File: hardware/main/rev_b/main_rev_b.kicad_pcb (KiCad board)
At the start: 4 copper layers, 140 x 100 mm, 165 parts, among them J1 USB-C USB2, J10 SWD, J2 ESC_CAN_POWER, J30 GNSS_UFL, J40 915MHz_ANT, Q30 2N7002, U1 USBLC6-2SC6, U10 RP2354B, U2 TLV62569DBVR, U20 ICM-42688-P, U21 LSM6DSO32TR, U22 LPS22DFTR, U3 TLV75528PDBVR, U30 LG77LICMD, U4 TLV75533PDBVR, U40 CC1121RHBR, U41 CC1190RGVR, U50 TCAN3413DR, U51 MCP2518FD-H/QBB, Y1 12MHz ABM8-272-T3, Y40 32MHz NT2016SA-32M-TEE3017A, Y50 40MHz ABM8G

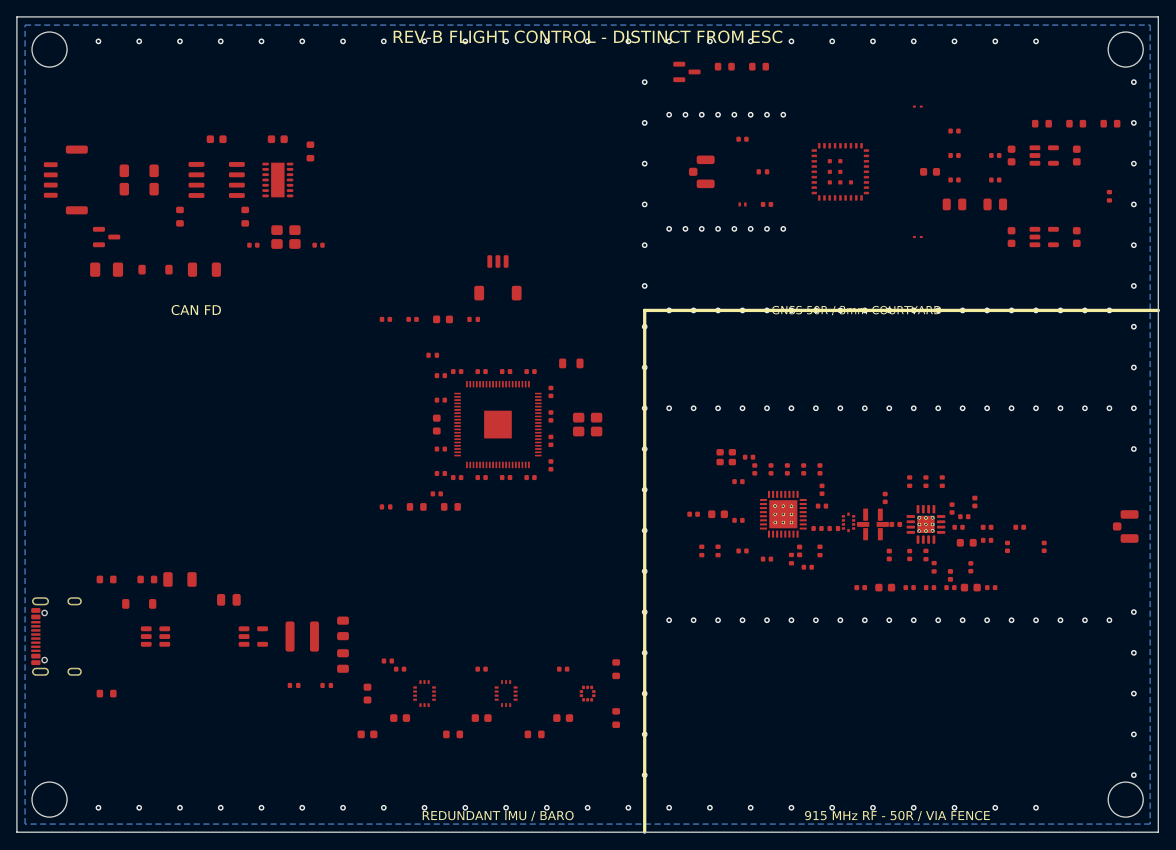
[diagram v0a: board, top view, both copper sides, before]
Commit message: main: FreeRouting signal routing imported (413->62 unrouted signals); cleanup slivers+dangling; 234 unconnected awaiting power zones
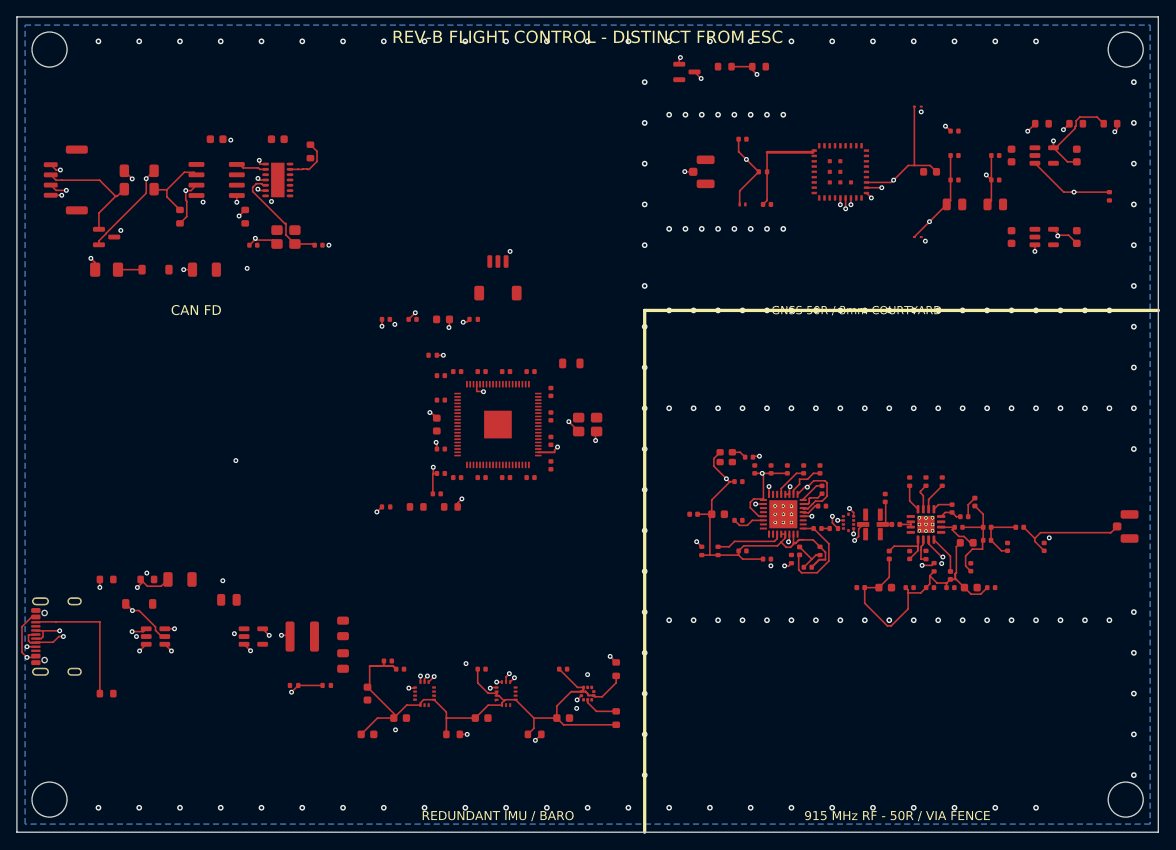
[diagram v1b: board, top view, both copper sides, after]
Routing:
- net /GNSS_PWR_EN: track 0.00 -> 94.3 mm, vias 0 -> 3
- net /915 MHz RF/VDD_CC112: track 0.00 -> 77.3 mm, vias 0 -> 4
- net /Redundant sensors/3V3_SENS: track 0.00 -> 75.1 mm
- net /GNSS/GNSS_RESET_OD: track 0.00 -> 65.9 mm, vias 0 -> 3
- net /USB_DP: track 0.00 -> 63.6 mm, vias 0 -> 3
- net /GNSS_RESET_N: track 0.00 -> 52.6 mm, vias 0 -> 2
- net /SENS_SCLK: track 0.00 -> 50.1 mm, vias 0 -> 3
- net /2V8_GNSS: track 0.00 -> 41.3 mm, vias 0 -> 3
- net /3V3_GNSS: track 0.00 -> 41.3 mm, vias 0 -> 3
- net /915 MHz RF/VDD_CC119: track 0.00 -> 36.6 mm
- net /GNSS/GNSS_VBCKP: track 0.00 -> 36.2 mm, vias 0 -> 2
- net /Power and USB/CHASSIS: track 0.00 -> 33.2 mm, vias 0 -> 1
- net /USB_DM: track 0.00 -> 32.8 mm, vias 0 -> 2
- net /RP2354B MCU/XOUT: track 0.00 -> 31.2 mm, vias 0 -> 2
- net /RP2354B MCU/XIN: track 0.00 -> 31.0 mm, vias 0 -> 2
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
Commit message: main: power planes (F.Cu+B.Cu GND, In1 3V3, In2 1V1) + 130 via drops + SYS_5V trunk; 234->~70 unconnected
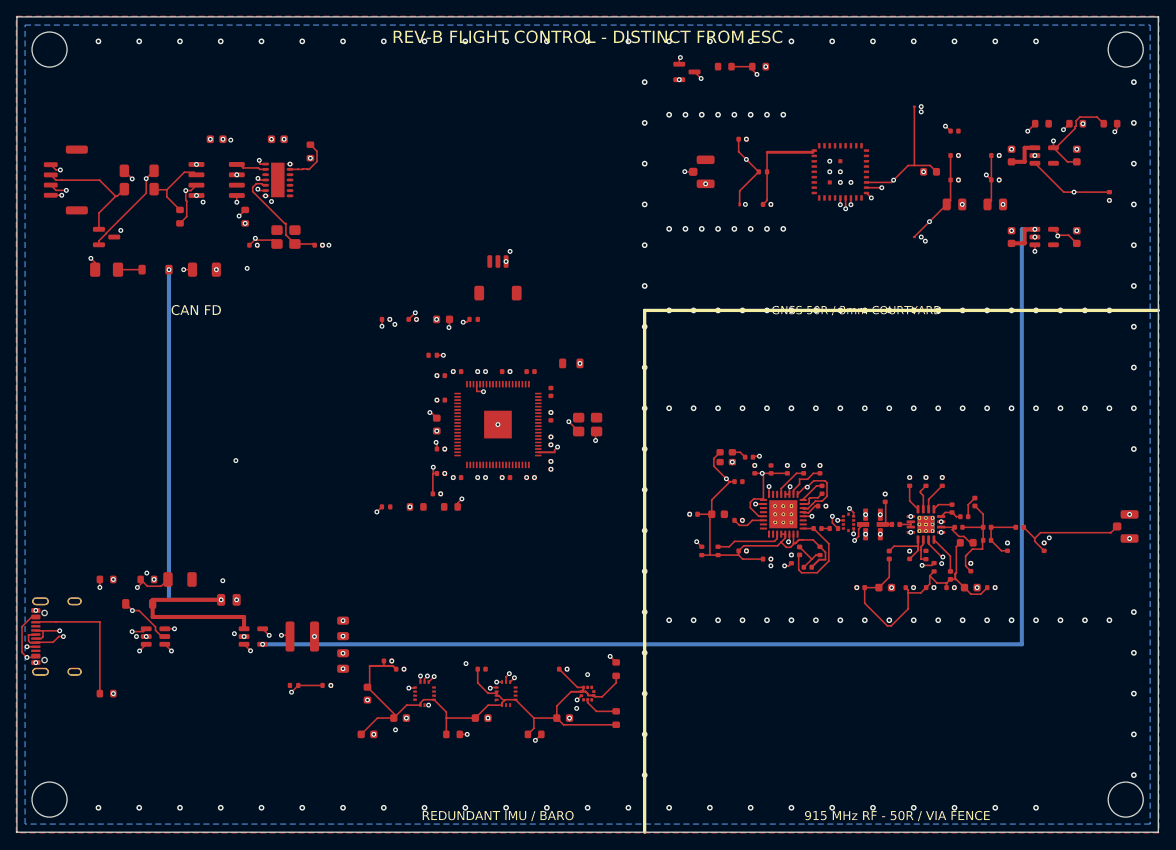
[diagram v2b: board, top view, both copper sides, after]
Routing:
- net /SYS_5V: track 0.00 -> 224.9 mm, vias 0 -> 4
- net /GND: vias 175 -> 276
- net /3V3: vias 0 -> 23
- net /1V1: vias 0 -> 5
- added copper zone on In2.Cu, net /1V1
- added copper zone on In1.Cu, net /3V3
- added copper zone on F.Cu, net /GND

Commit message: main: SYS_5V trunk routed obstacle-checked; 0 real violations, 70 unconnected (signal pads remain)
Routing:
- net /SYS_5V: track 224.9 -> 178.0 mm, vias 4 -> 2
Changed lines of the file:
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@@
 	)
 	(segment
-		(start 16.649999 71.5)
-		(end 16.649999 72)
+		(start 123.6 27.775)
+		(end 122 27.775)
+		(width 0.5)
+		(layer "F.Cu")
+		(net 107)
+	)
+	(segment
+		(start 25.05 71.5)
+		(end 16.649999 71.5)
+		(width 0.5)
+		(layer "F.Cu")
+		(net 107)
+	)
+	(segment
+		(start 16.649999 73.6)
+		(end 27.8625 73.6)
+		(width 0.5)
+		(layer "F.Cu")
+		(net 107)
+	)
+	(segment
+		(start 16.649999 72)
+		(end 16.649999 73.6)
+		(width 0.5)
+		(layer "F.Cu")
+		(net 107)
+	)
+	(segment
+		(start 124.8625 26.05)
+		(end 123.6 26.05)
+		(width 0.5)
+		(layer "F.Cu")
+		(net 107)
+	)
+	(segment
+		(start 123.6 16.05)
+		(end 124.8625 16.05)
 		(width 0.5)
 		(layer "F.Cu")
@@
 	)
 	(segment
-		(start 16.649999 72)
-		(end 16.649999 73.6)
+		(start 27.8625 73.6)
+		(end 27.8625 75.05)
+		(width 0.5)
+		(layer "F.Cu")
+		(net 107)
+	)
+	(segment
+		(start 16.649999 71.5)
+		(end 16.649999 72)
 		(width 0.5)
 		(layer "F.Cu")
@@
 	)
 	(segment
-		(start 16.649999 73.6)
-		(end 27.8625 73.6)
-		(width 0.5)
-		(layer "F.Cu")
-		(net 107)
-	)
-	(segment
 		(start 123.6 17.775)
 		(end 123.6 16.05)
@@
 		(net 107)
 	)
-	(segment
-		(start 123.6 16.05)
-		(end 124.8625 16.05)
-		(width 0.5)
-		(layer "F.Cu")
-		(net 107)
-	)
-	(segment
-		(start 123.6 27.775)
-		(end 122 27.775)
-		(width 0.5)
-		(layer "F.Cu")
-		(net 107)
-	)
-	(segment
-		(start 124.8625 26.05)
-		(end 123.6 26.05)
-		(width 0.5)
-		(layer "F.Cu")
-		(net 107)
-	)
-	(segment
-		(start 27.8625 73.6)
-		(end 27.8625 75.05)
-		(width 0.5)
-		(layer "F.Cu")
-		(net 107)
-	)
-	(segment
-		(start 25.05 71.5)
-		(end 16.649999 71.5)
-		(width 0.5)
-		(layer "F.Cu")
-		(net 107)
-	)
 	(via
-		(at 18.65 31)
+		(at 30.1375 76.95)
 		(size 0.6)
 		(drill 0.3)
@@
 		(net 107)
 	)
-	(via
-		(at 25.05 71.5)
-		(size 0.6)
-		(drill 0.3)
-		(layers "F.Cu" "B.Cu")
-		(net 107)
-	)
-	(via
-		(at 30.1375 76.95)
-		(size 0.6)
-		(drill 0.3)
-		(layers "F.Cu" "B.Cu")
-		(net 107)
-	)
 	(segment
-		(start 123.2625 26.05)
-		(end 124.8625 26.05)
+		(start 30.1375 76.95)
+		(end 123.2625 76.95)
 		(width 0.5)
 		(layer "B.Cu")
@@
 	)
 	(segment
-		(start 18.65 71.5)
-		(end 25.05 71.5)
+		(start 123.2625 26.05)
+		(end 124.8625 26.05)
 		(width 0.5)
 		(layer "B.Cu")
-		(net 107)
-	)
-	(segment
-		(start 30.1375 76.95)
-		(end 123.2625 76.95)
-		(width 0.5)
-		(layer "B.Cu")
-		(net 107)
-	)
-	(segment
-		(start 18.65 31)
-		(end 18.65 71.5)
-		(width 0.5)
-		(layer "B.Cu")

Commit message: pcb: manually route local rev b 3v3 connections
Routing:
- net /3V3: track 0.00 -> 1.95 mm
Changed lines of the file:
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@@
 		(net 2)
+	)
+	(segment
+		(start 59.6 45.05)
+		(end 59.52 43.5)
+		(width 0.2)
+		(layer "F.Cu")
+		(net 3)
+	)
+	(segment
+		(start 59.6 45.05)
+		(end 60 45.05)
+		(width 0.2)
+		(layer "F.Cu")
+		(net 3)
 	)
 	(via

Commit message: pcb: route additional local rev b 3v3 links
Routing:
- net /3V3: track 1.95 -> 12.5 mm
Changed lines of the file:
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@@
+	)
+	(segment
+		(start 61.6 44.3)
+		(end 62.52 44.3)
+		(width 0.2)
+		(layer "F.Cu")
+		(net 3)
+	)
+	(segment
+		(start 63.95 50.2)
+		(end 64.7 50.2)
+		(width 0.2)
+		(layer "F.Cu")
+		(net 3)
+	)
+	(segment
+		(start 56.8 44.2)
+		(end 56.52 44.2)
+		(width 0.2)
+		(layer "F.Cu")
+		(net 3)
+	)
+	(segment
+		(start 54.05 51.8)
+		(end 53.4 51.8)
+		(width 0.2)
+		(layer "F.Cu")
+		(net 3)
+	)
+	(segment
+		(start 53.4 51.8)
+		(end 51.5 50.7875)
+		(width 0.2)
+		(layer "F.Cu")
+		(net 3)
+	)
+	(segment
+		(start 61.6 45.05)
+		(end 61.6 44.3)
+		(width 0.2)
+		(layer "F.Cu")
+		(net 3)
+	)
+	(segment
+		(start 63.95 46.2)
+		(end 64.7 46.2)
+		(width 0.2)
+		(layer "F.Cu")
+		(net 3)
+	)
+	(segment
+		(start 56.52 44.2)
+		(end 56.52 43.5)
+		(width 0.2)
+		(layer "F.Cu")
+		(net 3)
 	)
 	(segment
@@
 		(width 0.2)
 		(layer "F.Cu")
+		(net 3)
+	)
+	(segment
+		(start 62.52 44.3)
+		(end 62.52 43.5)
+		(width 0.2)
+		(layer "F.Cu")
+		(net 3)
+	)
+	(segment
+		(start 56.8 45.05)
+		(end 56.8 44.2)
+		(width 0.2)
+		(layer "F.Cu")
+		(net 3)
+	)
+	(segment
+		(start 64.7 50.2)
+		(end 65.5 49.48)
+		(width 0.2)
+		(layer "F.Cu")
+		(net 3)
+	)
+	(segment
+		(start 64.7 46.2)
+		(end 65.5 46.48)
+		(width 0.2)
+		(layer "F.Cu")

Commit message: pcb: route local rev b 1v1 connection
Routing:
- net /1V1: track 0.00 -> 1.55 mm
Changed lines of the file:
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@@
 		)
+	)
+	(segment
+		(start 59.6 54.95)
+		(end 59.52 56.5)
+		(width 0.2)
+		(layer "F.Cu")
+		(net 1)
 	)
 	(via

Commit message: pcb: route local rev b r6 3v3 link
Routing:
- net /3V3: track 12.5 -> 19.2 mm
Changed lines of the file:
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@@
+	)
+	(segment
+		(start 33.49 82)
+		(end 36.5 76)
+		(width 0.2)
+		(layer "F.Cu")
+		(net 3)
 	)
 	(segment
